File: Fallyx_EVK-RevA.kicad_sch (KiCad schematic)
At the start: 0 parts

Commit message: continued design work
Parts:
- added J7, J8, J9: Conn_01x12_Pin, Connector_PinHeader_2.54mm:PinHeader_1x12_P2.54mm_Vertical, symbol Connector:Conn_01x12_Pin
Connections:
- new net 1V8: J7.1 (Pin_1), J9.1 (Pin_1)
- new net 5V_USB: J8.1 (Pin_1)
- new net BLE_UART_RX: J9.3 (Pin_3)
- new net BLE_UART_TX: J9.4 (Pin_4)
- new net GND: J7.2 (Pin_2), J8.2 (Pin_2), J9.2 (Pin_2)
- new net I2C1_SCL: J7.6 (Pin_6)
- new net I2C1_SDA: J7.5 (Pin_5)
- new net I2C2_SCL: J7.4 (Pin_4)
- new net I2C2_SDA: J7.3 (Pin_3)
- new net JTMS_SWCLK: J7.11 (Pin_11)
- new net JTMS_SWDIO: J7.12 (Pin_12)
- new net PA0: J8.5 (Pin_5)
- new net PA1: J8.6 (Pin_6)
- new net PA10: J8.10 (Pin_10)
- new net PA9: J8.9 (Pin_9)
- new net PB0: J8.7 (Pin_7)
- new net PB1: J8.8 (Pin_8)
- new net PB12: J9.5 (Pin_5)
- new net PB13: J9.6 (Pin_6)
- new net PC0: J8.3 (Pin_3)
- new net PC1: J8.4 (Pin_4)
- new net PC4: J9.10 (Pin_10)
- new net PC5: J9.11 (Pin_11)
- new net PC6: J9.12 (Pin_12)
- new net PD7: J9.9 (Pin_9)
- new net PE3: J9.7 (Pin_7)
- new net PE6: J8.11 (Pin_11)
- new net PE7: J8.12 (Pin_12)
- new net PE9: J9.8 (Pin_8)
- new net SPI1_MISO: J7.8 (Pin_8)
- new net SPI1_MOSI: J7.9 (Pin_9)
- new net SPI1_SCK: J7.7 (Pin_7)
- new net STM_nRST: J7.10 (Pin_10)
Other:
- added sheet Fallyx_EVK_5 (Fallyx_EVK_5.kicad_sch)
- added sheet Fallyx_EVK_6 (Fallyx_EVK_6.kicad_sch)
- note added: "BLE"
- note added: "POWER"
- note added: "STM32 HEADER"

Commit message: review edits
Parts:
- removed J7, J8, J9: Conn_01x12_Pin, Connector_PinHeader_2.54mm:PinHeader_1x12_P2.54mm_Vertical, symbol Connector:Conn_01x12_Pin
- added J14: Conn_02x18_Odd_Even, Connector_PinHeader_2.54mm:PinHeader_2x18_P2.54mm_Vertical, symbol Connector_Generic:Conn_02x18_Odd_Even
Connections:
- net 1V8: now also J14.1 (Pin_1), J14.2 (Pin_2)
- net 5V_USB: now also J14.4 (Pin_4)
- net BLE_UART_RX: now also J14.7 (Pin_7)
- net BLE_UART_TX: now also J14.9 (Pin_9)
- net GND: now also J14.3 (Pin_3), J14.5 (Pin_5), J14.6 (Pin_6)
- net I2C1_SCL: now also J14.14 (Pin_14)
- net I2C1_SDA: now also J14.12 (Pin_12)
- net I2C2_SCL: now also J14.10 (Pin_10)
- net I2C2_SDA: now also J14.8 (Pin_8)
- net JTMS_SWCLK: now also J14.34 (Pin_34)
- net JTMS_SWDIO: now also J14.36 (Pin_36)
- net PA0: now also J14.29 (Pin_29)
- net PA1: now also J14.31 (Pin_31)
- net PA10: now also J14.24 (Pin_24)
- net PA9: now also J14.22 (Pin_22)
- net PB0: now also J14.33 (Pin_33)
- net PB1: now also J14.35 (Pin_35)
- net PB12: now also J14.11 (Pin_11)
- net PB13: now also J14.13 (Pin_13)
- net PC0: now also J14.25 (Pin_25)
- net PC1: now also J14.27 (Pin_27)
- net PC4: now also J14.19 (Pin_19)
- net PC5: now also J14.21 (Pin_21)
- net PC6: now also J14.23 (Pin_23)
- net PD7: now also J14.30 (Pin_30)
- net PE3: now also J14.15 (Pin_15)
- net PE6: now also J14.26 (Pin_26)
- net PE7: now also J14.28 (Pin_28)
- net PE9: now also J14.17 (Pin_17)
- net SPI1_MISO: now also J14.18 (Pin_18)
- net SPI1_MOSI: now also J14.20 (Pin_20)
- net SPI1_SCK: now also J14.16 (Pin_16)
- net STM_nRST: now also J14.32 (Pin_32)

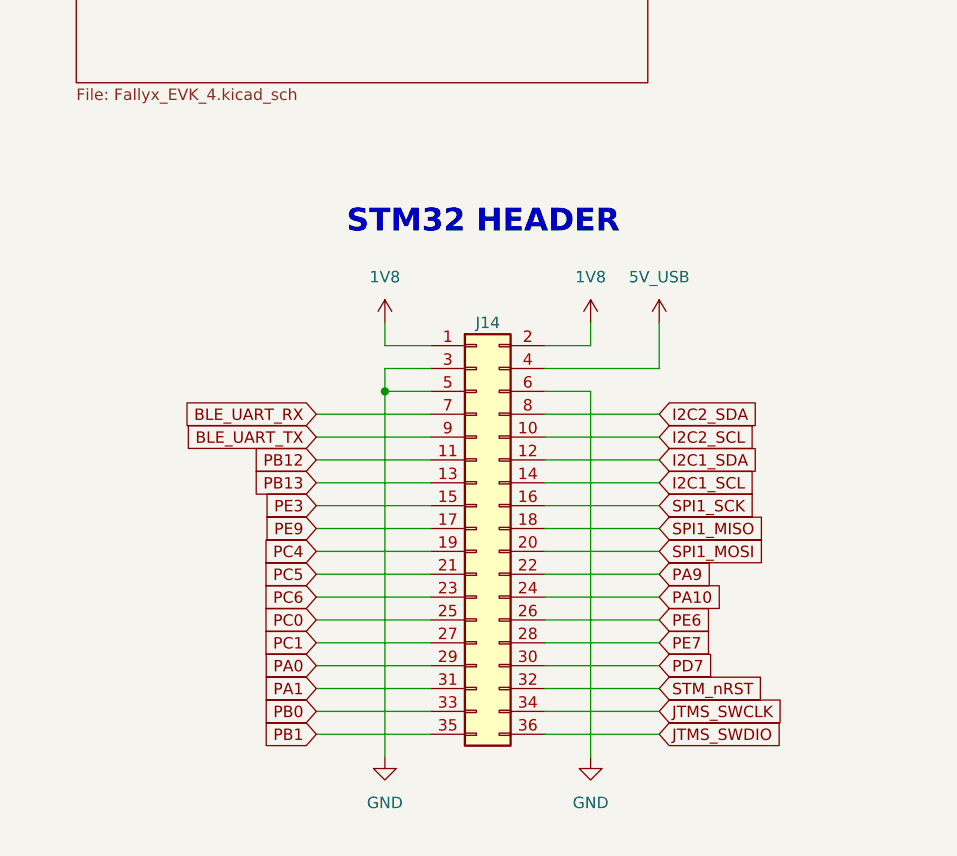
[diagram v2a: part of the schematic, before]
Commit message: Updated for new BLE modules
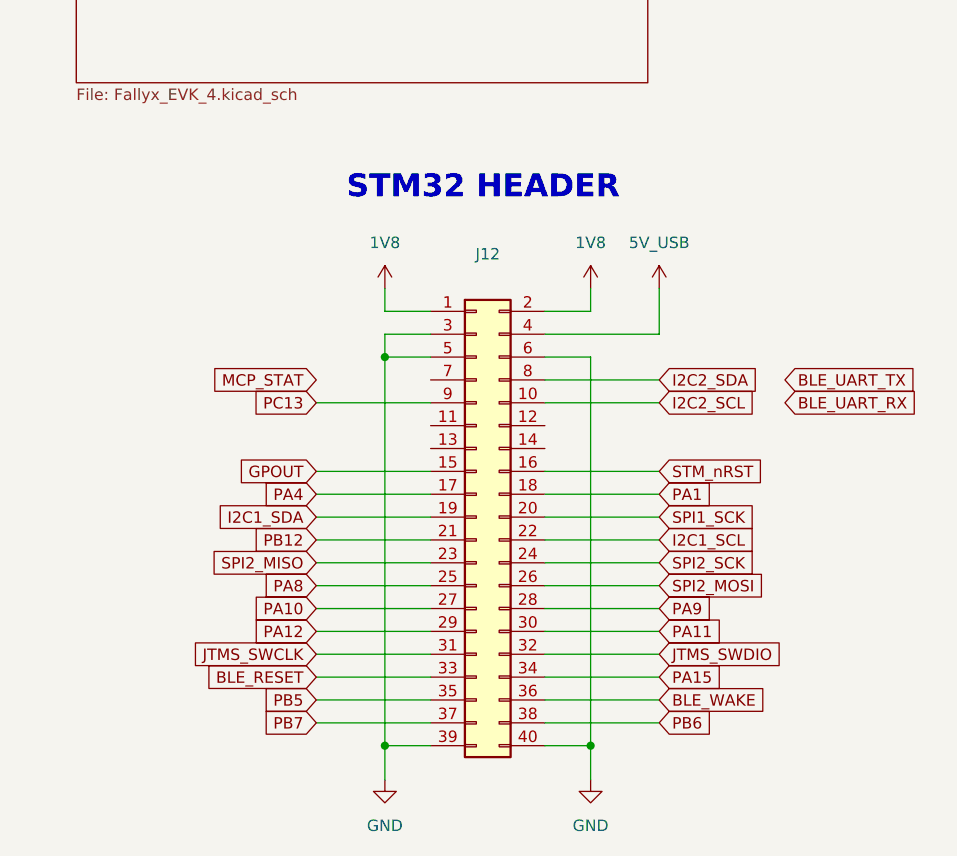
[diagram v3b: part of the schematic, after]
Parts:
- removed J14: Conn_02x18_Odd_Even, Connector_PinHeader_2.54mm:PinHeader_2x18_P2.54mm_Vertical, symbol Connector_Generic:Conn_02x18_Odd_Even
- added J12: Conn_02x20_Odd_Even, Connector_PinHeader_2.54mm:PinHeader_2x20_P2.54mm_Vertical, symbol Connector_Generic:Conn_02x20_Odd_Even
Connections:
- net 1V8: now also J12.1 (Pin_1), J12.2 (Pin_2)
- net 5V_USB: now also J12.4 (Pin_4)
- net GND: now also J12.3 (Pin_3), J12.39 (Pin_39), J12.40 (Pin_40), J12.5 (Pin_5), J12.6 (Pin_6)
- net I2C1_SCL: now also J12.22 (Pin_22)
- net I2C1_SDA: now also J12.19 (Pin_19)
- net I2C2_SCL: now also J12.10 (Pin_10)
- net I2C2_SDA: now also J12.8 (Pin_8)
- net JTMS_SWCLK: now also J12.31 (Pin_31)
- net JTMS_SWDIO: now also J12.32 (Pin_32)
- net PA1: now also J12.18 (Pin_18)
- net PA10: now also J12.27 (Pin_27)
- net PA9: now also J12.28 (Pin_28)
- net PB12: now also J12.21 (Pin_21)
- net SPI1_SCK: now also J12.20 (Pin_20)
- net STM_nRST: now also J12.16 (Pin_16)
- new net BLE_RESET: J12.33 (Pin_33)
- new net BLE_WAKE: J12.36 (Pin_36)
- new net GPOUT: J12.15 (Pin_15)
- new net PA11: J12.30 (Pin_30)
- new net PA12: J12.29 (Pin_29)
- new net PA15: J12.34 (Pin_34)
- new net PA4: J12.17 (Pin_17)
- new net PA8: J12.25 (Pin_25)
- new net PB5: J12.35 (Pin_35)
- new net PB6: J12.38 (Pin_38)
- new net PB7: J12.37 (Pin_37)
- new net PC13: J12.9 (Pin_9)
- new net SPI2_MISO: J12.23 (Pin_23)
- new net SPI2_MOSI: J12.26 (Pin_26)
- new net SPI2_SCK: J12.24 (Pin_24)
